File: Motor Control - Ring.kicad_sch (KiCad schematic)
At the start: 0 parts

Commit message: Update Schematic
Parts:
- added C56: 4.7uF 16V 0402, Duc_Library:C0402, symbol Duc-Capacitors:CAP CER 0402
- added C57: 100nF 16V 0603, Duc_Library:C0402, symbol Duc-Capacitors:CAP CER 0402
- added C58: 100nF 16V 0402, Duc_Library:C0402, symbol Duc-Capacitors:CAP CER 0402
- added C59: 470nF 16V 0402, Duc_Library:C0402, symbol Duc-Capacitors:CAP CER 0402
- added J4: BM09B-SRSS-TB, Duc:CONN-SMD_9P-P1.00_BM09B-SRSS-TB, symbol Duc-Connectors:BM09B-SRSS-TB
- added R13: 1R 0.1% 0402, Duc_Library:R0402, symbol Duc-Resistors:RES SMD 0402
- added R14: 10K 0.1% 0402, Duc_Library:R0402, symbol Duc-Resistors:RES SMD 0402
- added R15: 510R 0.1% 0402, Duc_Library:R0402, symbol Duc-Resistors:RES SMD 0402
- added U12: TB9051FTG,EL, Duc_Library:UQFN-28_L6.0-W6.0-P0.65-BL-EP4.0, symbol Duc-ICs:TB9051FTG,EL
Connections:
- new net: R14.1, R15.1
- new net +3.3V: J4.3, J4.8
- new net +5V: C56.2, J4.10, J4.11, R13.1
- new net +VBAT: C58.2, U12.11 (VBAT), U12.12 (VBAT), U12.24 (VBAT), U12.25 (VBAT)
- new net DGND: C56.1, C57.1, C59.1, R15.2, U12.1 (OCC), U12.27 (TEST1), U12.28 (TEST2), U12.3 (ENB), U12.4 (AGND)
- new net DIAG_M: U12.18 (DIAG)
- new net ECA_M: J4.6
- new net ECB_M: J4.7
- new net ECC_M: J4.2
- new net EN_M: U12.5 (EN)
- new net GND: C58.1, J4.1, J4.5, U12.15 (PGND), U12.16 (PGND), U12.17 (PGND), U12.19 (PGND), U12.20 (PGND), U12.21 (PGND), U12.29 (EP)
- new net OUT1_M: J4.4, U12.13 (OUT1), U12.14 (OUT1)
- new net OUT2_M: J4.9, U12.22 (OUT2), U12.23 (OUT2)
- new net PWMA_M: U12.8 (PWM1)
- new net PWMB_M: U12.9 (PWM2)
- new net VCC_M: C57.2, R13.2, U12.2 (VCC)
- new net _OCM_M: C59.2, R14.2, U12.7 (OCM)
- no-connect marks 0 -> 3

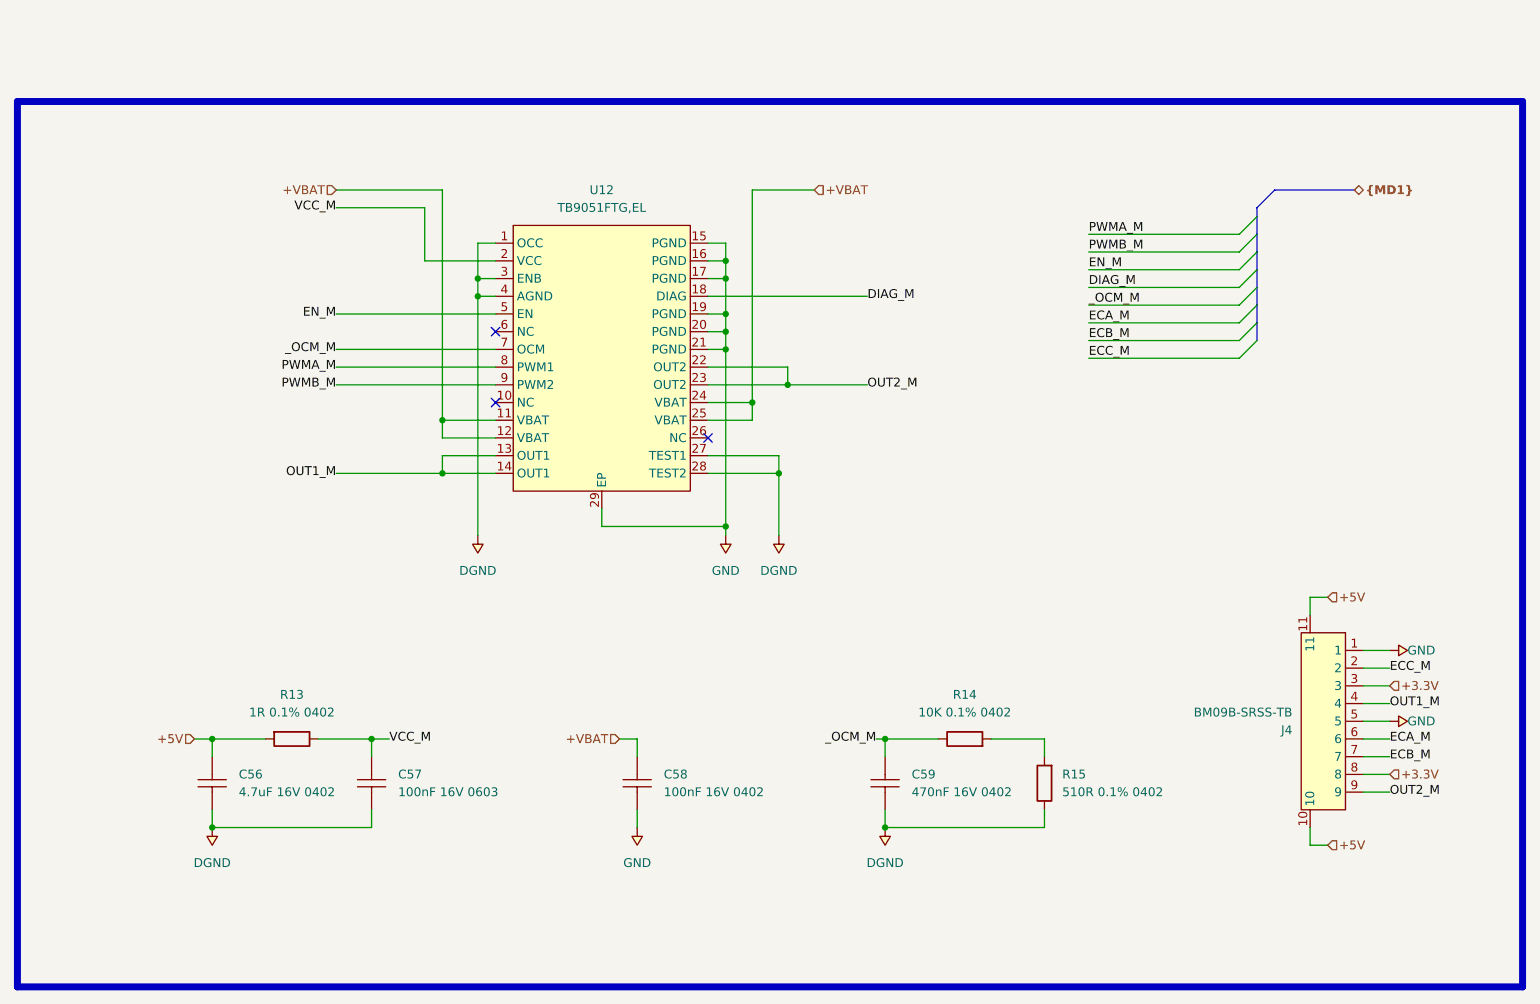
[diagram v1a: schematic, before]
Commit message: Update Motor Schematic
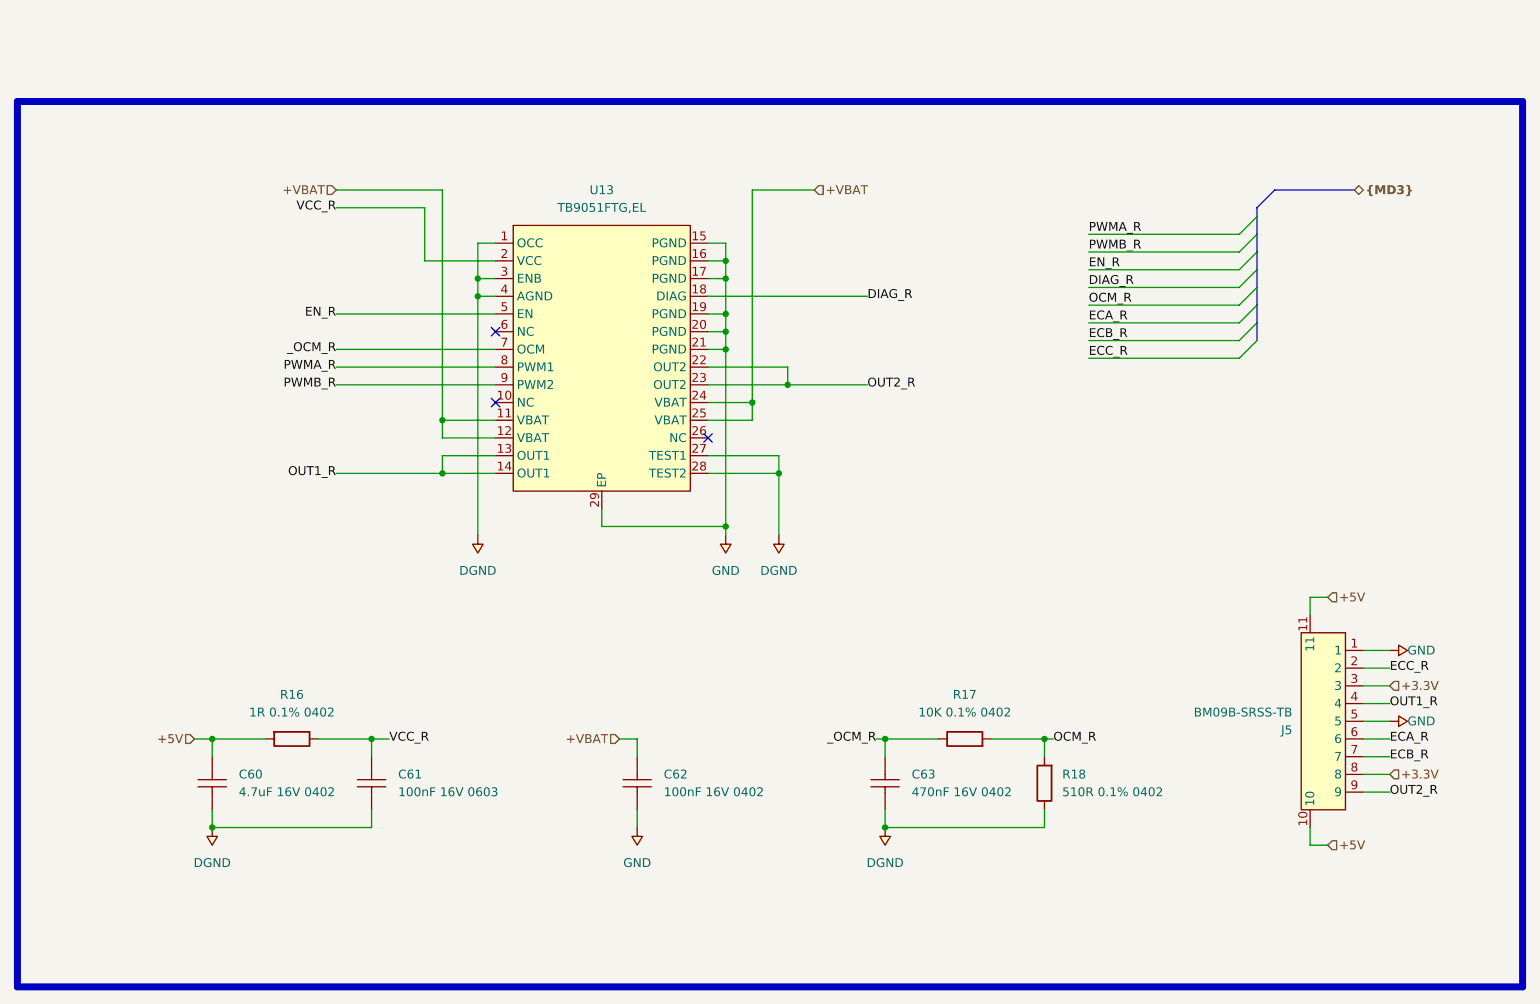
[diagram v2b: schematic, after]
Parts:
- removed C56: 4.7uF 16V 0402, Duc_Library:C0402, symbol Duc-Capacitors:CAP CER 0402
- removed C57: 100nF 16V 0603, Duc_Library:C0402, symbol Duc-Capacitors:CAP CER 0402
- removed C58: 100nF 16V 0402, Duc_Library:C0402, symbol Duc-Capacitors:CAP CER 0402
- removed C59: 470nF 16V 0402, Duc_Library:C0402, symbol Duc-Capacitors:CAP CER 0402
- removed J4: BM09B-SRSS-TB, Duc:CONN-SMD_9P-P1.00_BM09B-SRSS-TB, symbol Duc-Connectors:BM09B-SRSS-TB
- removed R13: 1R 0.1% 0402, Duc_Library:R0402, symbol Duc-Resistors:RES SMD 0402
- removed R14: 10K 0.1% 0402, Duc_Library:R0402, symbol Duc-Resistors:RES SMD 0402
- removed R15: 510R 0.1% 0402, Duc_Library:R0402, symbol Duc-Resistors:RES SMD 0402
- removed U12: TB9051FTG,EL, Duc_Library:UQFN-28_L6.0-W6.0-P0.65-BL-EP4.0, symbol Duc-ICs:TB9051FTG,EL
- added C60: 4.7uF 16V 0402, Duc_Library:C0402, symbol Duc-Capacitors:CAP CER 0402
- added C61: 100nF 16V 0603, Duc_Library:C0402, symbol Duc-Capacitors:CAP CER 0402
- added C62: 100nF 16V 0402, Duc_Library:C0402, symbol Duc-Capacitors:CAP CER 0402
- added C63: 470nF 16V 0402, Duc_Library:C0402, symbol Duc-Capacitors:CAP CER 0402
- added J5: BM09B-SRSS-TB, Duc:CONN-SMD_9P-P1.00_BM09B-SRSS-TB, symbol Duc-Connectors:BM09B-SRSS-TB
- added R16: 1R 0.1% 0402, Duc_Library:R0402, symbol Duc-Resistors:RES SMD 0402
- added R17: 10K 0.1% 0402, Duc_Library:R0402, symbol Duc-Resistors:RES SMD 0402
- added R18: 510R 0.1% 0402, Duc_Library:R0402, symbol Duc-Resistors:RES SMD 0402
- added U13: TB9051FTG,EL, Duc_Library:UQFN-28_L6.0-W6.0-P0.65-BL-EP4.0, symbol Duc-ICs:TB9051FTG,EL
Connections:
- net +3.3V: now also J5.3, J5.8
- net +5V: now also C60.2, J5.10, J5.11, R16.1
- net +VBAT: now also C62.2, U13.11 (VBAT), U13.12 (VBAT), U13.24 (VBAT), U13.25 (VBAT)
- net DGND: now also C60.1, C61.1, C63.1, R18.2, U13.1 (OCC), U13.27 (TEST1), U13.28 (TEST2), U13.3 (ENB), U13.4 (AGND)
- net GND: now also C62.1, J5.1, J5.5, U13.15 (PGND), U13.16 (PGND), U13.17 (PGND), U13.19 (PGND), U13.20 (PGND), U13.21 (PGND), U13.29 (EP)
- new net DIAG_R: U13.18 (DIAG)
- new net ECA_R: J5.6
- new net ECB_R: J5.7
- new net ECC_R: J5.2
- new net EN_R: U13.5 (EN)
- new net OCM_R: R17.1, R18.1
- new net OUT1_R: J5.4, U13.13 (OUT1), U13.14 (OUT1)
- new net OUT2_R: J5.9, U13.22 (OUT2), U13.23 (OUT2)
- new net PWMA_R: U13.8 (PWM1)
- new net PWMB_R: U13.9 (PWM2)
- new net VCC_R: C61.2, R16.2, U13.2 (VCC)
- new net _OCM_R: C63.2, R17.2, U13.7 (OCM)

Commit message: Update Schematic
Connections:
- net DGND is gone; now on net GND: C60.1, C61.1, C63.1, R18.2, U13.1 (OCC), U13.27 (TEST1), U13.28 (TEST2), U13.3 (ENB), U13.4 (AGND)

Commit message: Update Schematic
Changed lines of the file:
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@@
+	)
+	(rectangle
+		(start 177.8 25.4)
+		(end 254 76.2)
+		(stroke
+			(width 1)
+			(type default)
+			(color 200 0 0 1)
+		)
+		(fill
+			(type none)
+		)
 	)
 	(rectangle

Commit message: Update Schematic
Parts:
- added C90, C91: 100nF 16V 0402, Duc_Library:C0402, symbol Duc-Capacitors:CAP CER 0402
- added R63: 1K 0.1% 0402, Duc_Library:R0402, symbol Duc-Resistors:RES SMD 0402
- added R64, R73: 220R 0.1% 0402, Duc_Library:R0402, symbol Duc-Resistors:RES SMD 0402
- R14: renamed from R17; value 10K 0.1% 0402 -> 1K 0.1% 0402
- R15: renamed from R18; value 510R 0.1% 0402 -> 220R 0.1% 0402
- renumbered C60 to C56, C61 to C57, C62 to C58, C63 to C59, R16 to R13, U13 to U10
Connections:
- net +5V: no longer J5.10, J5.11
- net DIAG_R: now also R64.2; no longer U10.18 (DIAG)
- net ECC_R: now also C91.2, R73.2; no longer J5.2
- net GND: now also J5.10, J5.11, C90.1, C91.1
- net +3.3V renamed +3V3
- net +3V3: now also R63.2; no longer J5.3
- new net +A3V3: C90.2, J5.3
- new net _DIAG_R: R63.1, R64.1, U10.18 (DIAG)
- new net _ECC_R: J5.2, R73.1
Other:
- moved on the sheet: C56, C57, C58, C59, R13, R14, R15

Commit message: Update Schematic
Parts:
- renumbered C56 to C64, C57 to C65, C58 to C66, C59 to C67, C90 to C68, C91 to C69, R13 to R19, R14 to R20, R64 to R21, R15 to R22, R63 to R23, R73 to R24

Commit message: Update Schematic
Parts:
- C64: value 4.7uF 16V 0402 -> CAP CER 0402
- C65: value 100nF 16V 0603 -> CAP CER 0402
- C66, C68, C69: value 100nF 16V 0402 -> CAP CER 0402
- C67: value 470nF 16V 0402 -> CAP CER 0402
- R19: value 1R 0.1% 0402 -> RES 0402
- R20, R23: value 1K 0.1% 0402 -> RES 0402
- R21, R22, R24: value 220R 0.1% 0402 -> RES 0402

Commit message: Update Schematic
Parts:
- removed C64, C65, C66, C67, C68, C69: CAP CER 0402, Duc_Library:C0402, symbol Duc-Capacitors:CAP CER 0402
- removed R19, R20, R21, R22, R23, R24: RES 0402, Duc_Library:R0402, symbol Duc-Resistors:RES SMD 0402
- added C64: 4.7uF 50V 0603, Duc:C0603, symbol Duc-Capacitors:CAP CER 0603
- added C65, C66, C68, C69: 100nF 50V 0603, Duc:C0603, symbol Duc-Capacitors:CAP CER 0603
- added C67: 470nF 50V 0603, Duc:C0603, symbol Duc-Capacitors:CAP CER 0603
- added R19: 1R 0.1% 0603, Duc:R0603, symbol Duc-Resistors:RES SMD 0603
- added R20, R23: 1K 0.1% 0603, Duc:R0603, symbol Duc-Resistors:RES SMD 0603
- added R21, R22, R24: 220R 0.1% 0603, Duc:R0603, symbol Duc-Resistors:RES SMD 0603
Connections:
- net +3V3: now also R23.2
- net +5V: now also C64.2, R19.1
- net +A3V3: now also C68.2
- net +VBAT: now also C66.2
- net DIAG_R: now also R21.2
- net ECC_R: now also C69.2, R24.2
- net GND: now also C64.1, C65.1, C66.1, C67.1, C68.1, C69.1, R22.2
- net OCM_R: now also R20.1, R22.1
- net VCC_R: now also C65.2, R19.2
- net _DIAG_R: now also R21.1, R23.1
- net _ECC_R: now also R24.1
- net _OCM_R: now also C67.2, R20.2
